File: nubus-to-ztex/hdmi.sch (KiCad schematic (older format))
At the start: 10 parts, among them J5 HDMI_A, U9 TPD12S016PWR

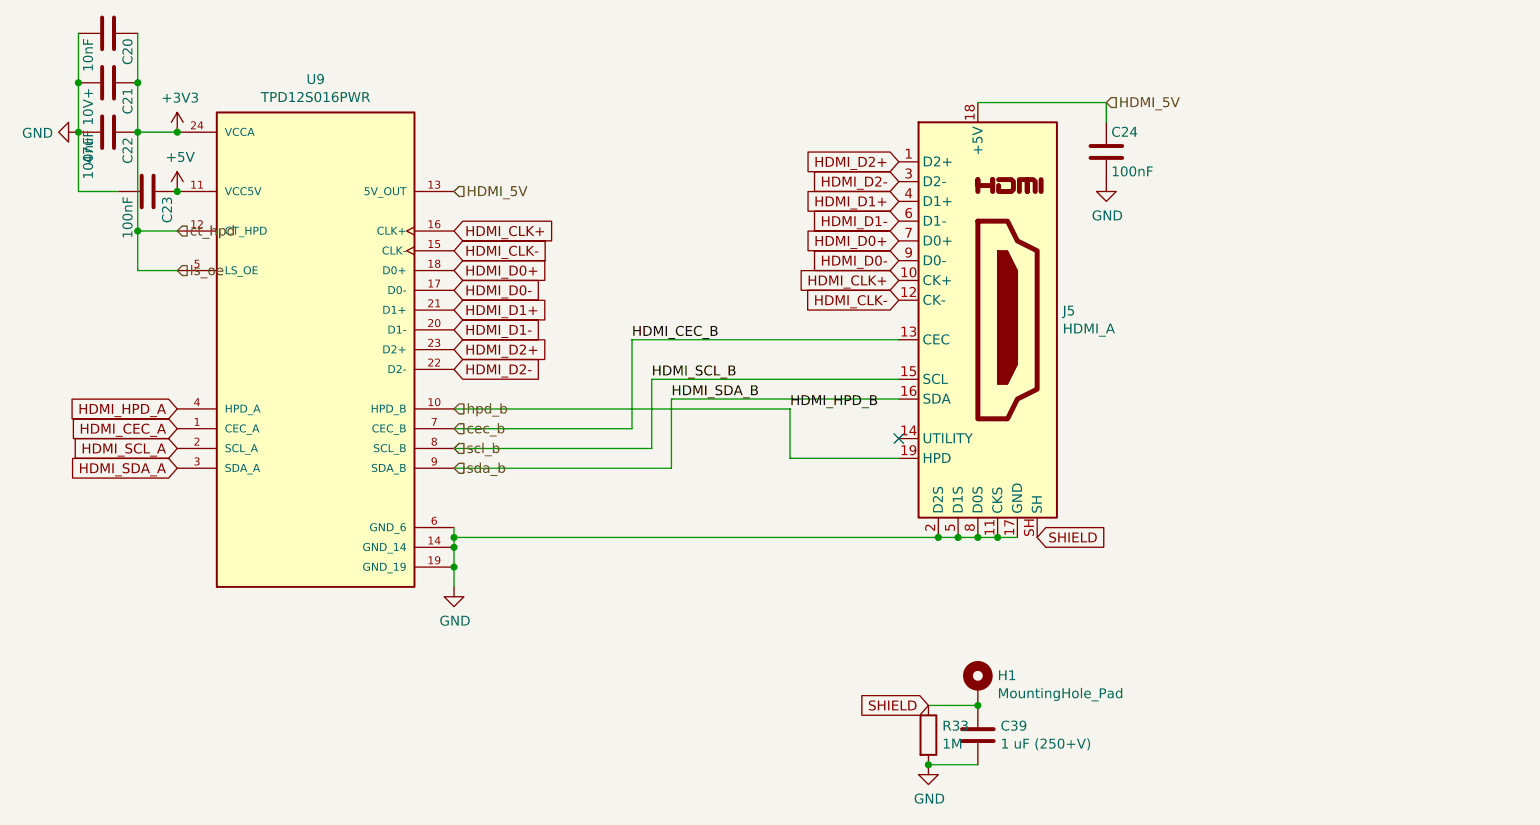
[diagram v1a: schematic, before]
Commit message: more update to V1.2 to try to limit cost
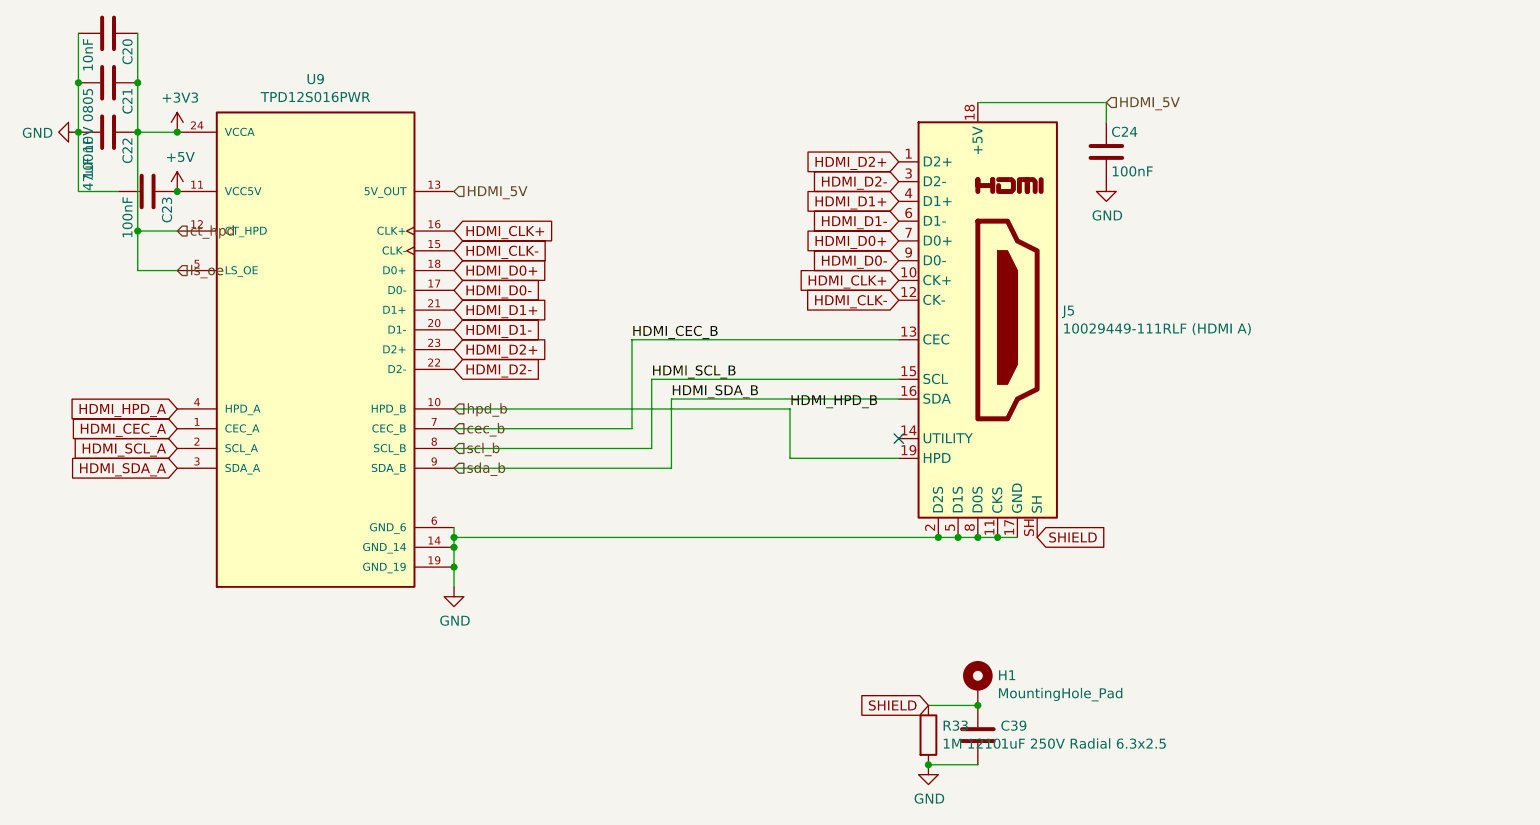
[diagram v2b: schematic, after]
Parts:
- C21: value 47uF 10V+ -> 47uF 10V 0805
- C39: value 1 uF (250+V) -> 1uF 250V Radial 6.3x2.5
- J5: value HDMI_A -> 10029449-111RLF (HDMI A)
- R33: value 1M -> 1M 1210
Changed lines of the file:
@@
 P 6650 2550
 F 0 "J5" H 7079 2596 50  0000 L CNN
-F 1 "HDMI_A" H 7079 2505 50  0000 L CNN
+F 1 "10029449-111RLF (HDMI A)" H 7079 2505 50  0000 L CNN
 F 2 "For_SeeedStudio:HDMI_A_Amphenol_10029449-111" H 6675 2550 50  0001 C CNN
 F 3 "https://en.wikipedia.org/wiki/HDMI" H 6675 2550 50  0001 C CNN
@@
 AR Path="/61B62C00/6148D34D" Ref="C21"  Part="1"
 F 0 "C21" H 2275 1450 50  0000 L CNN
-F 1 "47uF 10V+" H 2275 1250 50  0000 L CNN
+F 1 "47uF 10V 0805" H 2275 1250 50  0000 L CNN
 F 2 "Capacitor_SMD:C_0805_2012Metric" H 2288 1200 50  0001 C CNN
 F 3 "" H 2250 1350 50  0000 C CNN
@@
 AR Path="/61B62C00/63467FEB" Ref="C39"  Part="1"
 F 0 "C39" H 6765 4696 50  0000 L CNN
-F 1 "1 uF (250+V)" H 6765 4605 50  0000 L CNN
+F 1 "1uF 250V Radial 6.3x2.5" H 6765 4605 50  0000 L CNN
 F 2 "Capacitor_THT:CP_Radial_D6.3mm_P2.50mm" H 6688 4500 50  0001 C CNN
 F 3 "~" H 6650 4650 50  0001 C CNN
@@
 AR Path="/61B62C00/63467FF7" Ref="R33"  Part="1"
 F 0 "R33" H 6470 4696 50  0000 L CNN
-F 1 "1M" H 6470 4605 50  0000 L CNN
+F 1 "1M 1210" H 6470 4605 50  0000 L CNN
 F 2 "Resistor_SMD:R_1210_3225Metric" V 6330 4650 50  0001 C CNN
 F 3 "~" H 6400 4650 50  0001 C CNN

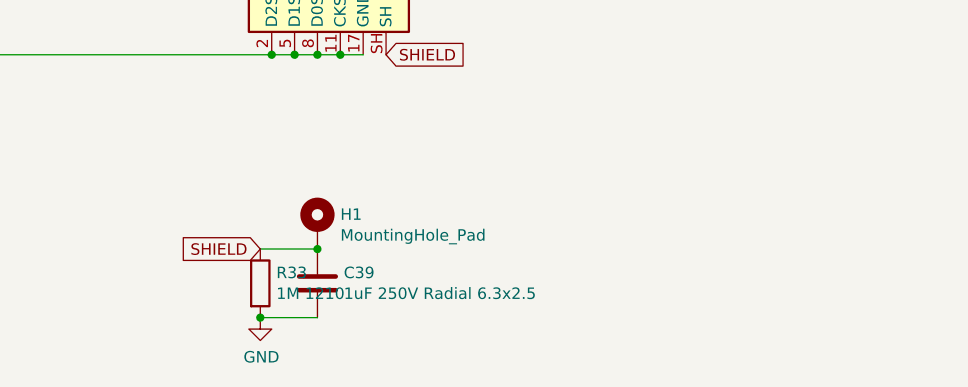
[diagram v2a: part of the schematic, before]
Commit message: more THT->SMT, lexx expensive parts/assembly (?)
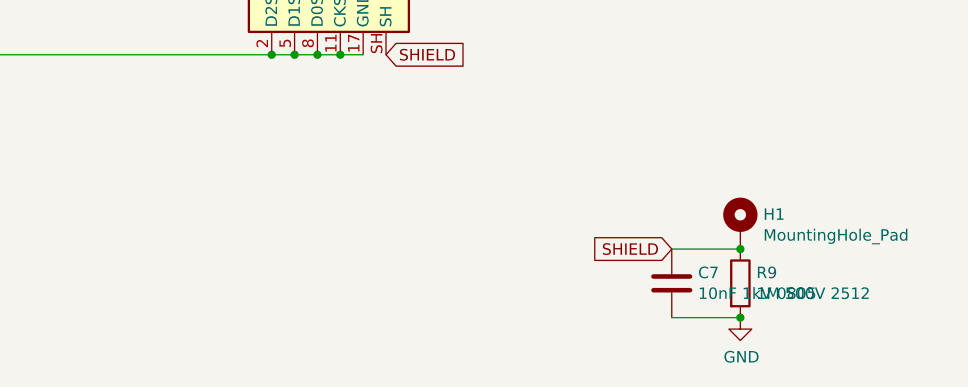
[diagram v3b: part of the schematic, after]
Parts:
- removed C39: 1uF 250V Radial 6.3x2.5, Capacitor_THT:CP_Radial_D6.3mm_P2.50mm, symbol Device:C
- removed R33: 1M 1210, Resistor_SMD:R_1210_3225Metric, symbol Device:R
- added C7: 10nF 1kV 0805, Capacitor_SMD:C_0805_2012Metric, symbol Device:C
- added R9: 1M 500V 2512, Resistor_SMD:R_2512_6332Metric, symbol Device:R
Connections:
- net GND: now also C7.2, R9.2
- net SHIELD: now also C7.1, R9.1
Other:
- moved on the sheet: H1
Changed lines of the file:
@@
 Text HLabel 4000 1900 2    50   Input ~ 0
 HDMI_5V
-Text GLabel 6400 4500 0    50   Input ~ 0
+Text GLabel 8200 4500 0    50   Input ~ 0
 SHIELD
 $Comp
+L Mechanical:MountingHole_Pad H?
+U 1 1 63467FFE
+P 8500 4400
+AR Path="/6193AB43/63467FFE" Ref="H?"  Part="1"
+AR Path="/61B62C00/63467FFE" Ref="H1"  Part="1"
+F 0 "H1" H 8600 4451 50  0000 L CNN
+F 1 "MountingHole_Pad" H 8600 4360 50  0000 L CNN
+F 2 "MountingHole:MountingHole_2.2mm_M2_Pad" H 8500 4400 50  0001 C CNN
+F 3 "~" H 8500 4400 50  0001 C CNN
+	1    8500 4400
+	1    0    0    -1
+$EndComp
+$Comp
 L power:GND #PWR?
-U 1 1 63467FDF
-P 6400 4800
-AR Path="/6193AB43/63467FDF" Ref="#PWR?"  Part="1"
-AR Path="/61B62C00/63467FDF" Ref="#PWR0132"  Part="1"
-F 0 "#PWR0132" H 6400 4550 50  0001 C CNN
-F 1 "GND" H 6405 4627 50  0000 C CNN
-F 2 "" H 6400 4800 50  0001 C CNN
-F 3 "" H 6400 4800 50  0001 C CNN
-	1    6400 4800
+U 1 1 641A2752
+P 8500 4800
+AR Path="/61B62C00/641A0A1A/641A2752" Ref="#PWR?"  Part="1"
+AR Path="/61B62C00/641A2752" Ref="#PWR0132"  Part="1"
+F 0 "#PWR0132" H 8500 4550 50  0001 C CNN
+F 1 "GND" H 8505 4627 50  0000 C CNN
+F 2 "" H 8500 4800 50  0001 C CNN
+F 3 "" H 8500 4800 50  0001 C CNN
+	1    8500 4800
+	1    0    0    -1
+$EndComp
+$Comp
+L Device:C C?
+U 1 1 641A275A
+P 8200 4650
+AR Path="/61B62C00/641A0A1A/641A275A" Ref="C?"  Part="1"
+AR Path="/61B62C00/641A275A" Ref="C7"  Part="1"
+F 0 "C7" H 8315 4696 50  0000 L CNN
+F 1 "10nF 1kV 0805" H 8315 4605 50  0000 L CNN
+F 2 "Capacitor_SMD:C_0805_2012Metric" H 8238 4500 50  0001 C CNN
+F 3 "~" H 8200 4650 50  0001 C CNN
+F 4 "C0805V103KCRACTU" H 8200 4650 50  0001 C CNN "MPN"
+F 5 "https://www.lcsc.com/product-detail/Multilayer-Ceramic-Capacitors-MLCC-SMD-SMT_KEMET-C0805V103KCRACTU_C2170011.html" H 8200 4650 50  0001 C CNN "URL"
+	1    8200 4650
 	1    0    0    -1
 $EndComp
 Wire Wire Line
-	6650 4800 6400 4800
-Wire Wire Line
-	6650 4500 6400 4500
+	8500 4800 8200 4800
 $Comp
-L Device:C C?
-U 1 1 63467FEB
-P 6650 4650
-AR Path="/6193AB43/63467FEB" Ref="C?"  Part="1"
-AR Path="/61B62C00/63467FEB" Ref="C39"  Part="1"
-F 0 "C39" H 6765 4696 50  0000 L CNN
-F 1 "1uF 250V Radial 6.3x2.5" H 6765 4605 50  0000 L CNN
-F 2 "Capacitor_THT:CP_Radial_D6.3mm_P2.50mm" H 6688 4500 50  0001 C CNN
-F 3 "~" H 6650 4650 50  0001 C CNN
-F 4 "860021373002" H 6650 4650 50  0001 C CNN "MPN-ALT"
-F 5 "https://www2.mouser.com/ProductDetail/Wurth-Elektronik/860021373002?qs=0KOYDY2FL28tNXbPyU6hsg%3D%3D" H 6650 4650 50  0001 C CNN "URL-ALT"
-F 6 "KM010M400E110A" H 6650 4650 50  0001 C CNN "MPN"
-F 7 "https://lcsc.com/product-detail/Aluminum-Electrolytic-Capacitors-Leaded_Capxon-International-Elec-KM010M400E110A_C59365.html" H 6650 4650 50  0001 C CNN "URL"
-	1    6650 4650
+L Device:R R?
+U 1 1 641A2763
+P 8500 4650
+AR Path="/61B62C00/641A0A1A/641A2763" Ref="R?"  Part="1"
+AR Path="/61B62C00/641A2763" Ref="R9"  Part="1"
+F 0 "R9" H 8570 4696 50  0000 L CNN
+F 1 "1M 500V 2512" H 8570 4605 50  0000 L CNN
+F 2 "Resistor_SMD:R_2512_6332Metric" V 8430 4650 50  0001 C CNN
+F 3 "~" H 8500 4650 50  0001 C CNN
+F 4 "AS25J1004ET" H 8500 4650 50  0001 C CNN "MPN"
+F 5 "https://www.lcsc.com/product-detail/Chip-Resistor-Surface-Mount_Ohmite-AS25J1004ET_C2546765.html" H 8500 4650 50  0001 C CNN "URL"
+	1    8500 4650
 	1    0    0    -1
 $EndComp
-Connection ~ 6400 4800
-$Comp
-L Device:R R?
-U 1 1 63467FF7
-P 6400 4650
-AR Path="/6193AB43/63467FF7" Ref="R?"  Part="1"
-AR Path="/61B62C00/63467FF7" Ref="R33"  Part="1"
-F 0 "R33" H 6470 4696 50  0000 L CNN
-F 1 "1M 1210" H 6470 4605 50  0000 L CNN
-F 2 "Resistor_SMD:R_1210_3225Metric" V 6330 4650 50  0001 C CNN
-F 3 "~" H 6400 4650 50  0001 C CNN
-F 4 "RC1210FR-071ML" H 6400 4650 50  0001 C CNN "MPN-ALT"
-F 5 "https://lcsc.com/product-detail/Chip-Resistor-Surface-Mount_YAGEO-RC1210FR-071ML_C470029.html" H 6400 4650 50  0001 C CNN "URL-ALT"
-F 6 "1210W2F1004T5E" H 6400 4650 50  0001 C CNN "MPN"
-F 7 "https://www.lcsc.com/product-detail/Chip-Resistor-Surface-Mount_UNI-ROYAL-Uniroyal-Elec-1210W2F1004T5E_C620664.html" H 6400 4650 50  0001 C CNN "URL"
-	1    6400 4650
-	1    0    0    -1
-$EndComp
-$Comp
-L Mechanical:MountingHole_Pad H?
-U 1 1 63467FFE
-P 6650 4400
-AR Path="/6193AB43/63467FFE" Ref="H?"  Part="1"
-AR Path="/61B62C00/63467FFE" Ref="H1"  Part="1"
-F 0 "H1" H 6750 4451 50  0000 L CNN
-F 1 "MountingHole_Pad" H 6750 4360 50  0000 L CNN
-F 2 "MountingHole:MountingHole_2.2mm_M2_Pad" H 6650 4400 50  0001 C CNN
-F 3 "~" H 6650 4400 50  0001 C CNN
-	1    6650 4400
-	1    0    0    -1
-$EndComp
-Connection ~ 6650 4500
+Connection ~ 8500 4800
+Wire Wire Line
+	8200 4500 8500 4500
+Connection ~ 8500 4500
 $EndSCHEMATC

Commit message: minor cleanups
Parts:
- C22, C23, C24: LCSC ? -> (none)
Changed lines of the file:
@@
 F 6 "603-CC603KRX7R8BB104" H 7300 1700 50  0001 C CNN "Mouser"
 F 7 "?" H 7300 1700 50  0001 C CNN "Digikey"
-F 8 "?" H 7300 1700 50  0001 C CNN "LCSC"
+F 8 "" H 7300 1700 50  0001 C CNN "LCSC"
 F 9 "?" H 7300 1700 50  0001 C CNN "Koncar"
 F 10 "TB" H 7300 1700 50  0001 C CNN "Side"
@@
 F 6 "603-CC603KRX7R8BB104" H 2250 1600 50  0001 C CNN "Mouser"
 F 7 "?" H 2250 1600 50  0001 C CNN "Digikey"
-F 8 "?" H 2250 1600 50  0001 C CNN "LCSC"
+F 8 "" H 2250 1600 50  0001 C CNN "LCSC"
 F 9 "?" H 2250 1600 50  0001 C CNN "Koncar"
 F 10 "TB" H 2250 1600 50  0001 C CNN "Side"
@@
 F 6 "603-CC603KRX7R8BB104" H 2450 1900 50  0001 C CNN "Mouser"
 F 7 "?" H 2450 1900 50  0001 C CNN "Digikey"
-F 8 "?" H 2450 1900 50  0001 C CNN "LCSC"
+F 8 "" H 2450 1900 50  0001 C CNN "LCSC"
 F 9 "?" H 2450 1900 50  0001 C CNN "Koncar"
 F 10 "TB" H 2450 1900 50  0001 C CNN "Side"

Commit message: BoM, power plane, serial back to THT, ...
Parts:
- C20, C22, C23, C24: URL https://lcsc.com/product-detail/Multilayer-Ceramic-Capacito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 -> https://www.lcsc.com/product-detail/Multilayer-Ceramic-Capa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
- C21: MPN GRM21BR61A476ME15K -> C2012X5R1A476MTJ00E; URL https://www.lcsc.com/product-detail/Multilayer-Ceramic-Capacitors-MLCC-SMD-SMT_Murata-Electronics-GRM21BR61A476ME15K_C2292827.html -> https://www.lcsc.com/product-detail/Multilayer-Ceramic-Capacitors-MLCC-SMD-SMT_TDK-C2012X5R1A476MTJ00E_C76636.html
- H1: DNP (none) -> DNP
- J5: URL https://lcsc.com/product-detail/D-Sub-DVI-HDMI-Connectors_A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 -> https://www.lcsc.com/product-detail/D-Sub-DVI-HDMI-Connecto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
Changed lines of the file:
@@
 F 9 "?" H 7300 1700 50  0001 C CNN "Koncar"
 F 10 "TB" H 7300 1700 50  0001 C CNN "Side"
-F 11 "https://lcsc.com/product-detail/Multilayer-Ceramic-Capacitors-MLCC-SMD-SMT_YAGEO-CC0603KRX7R8BB104_C92490.html" H 3000 6050 50  0001 C CNN "URL"
+F 11 "https://www.lcsc.com/product-detail/Multilayer-Ceramic-Capacitors-MLCC-SMD-SMT_YAGEO-CC0603KRX7R8BB104_C92490.html" H 3000 6050 50  0001 C CNN "URL"
 	1    7300 1700
 	1    0    0    -1
@@
 F 9 "?" H 2250 1600 50  0001 C CNN "Koncar"
 F 10 "TB" H 2250 1600 50  0001 C CNN "Side"
-F 11 "https://lcsc.com/product-detail/Multilayer-Ceramic-Capacitors-MLCC-SMD-SMT_YAGEO-CC0603KRX7R8BB104_C92490.html" H 2250 1600 50  0001 C CNN "URL"
+F 11 "https://www.lcsc.com/product-detail/Multilayer-Ceramic-Capacitors-MLCC-SMD-SMT_YAGEO-CC0603KRX7R8BB104_C92490.html" H 2250 1600 50  0001 C CNN "URL"
 	1    2250 1600
 	0    1    1    0
@@
 F 9 "?" H 2450 1900 50  0001 C CNN "Koncar"
 F 10 "TB" H 2450 1900 50  0001 C CNN "Side"
-F 11 "https://lcsc.com/product-detail/Multilayer-Ceramic-Capacitors-MLCC-SMD-SMT_YAGEO-CC0603KRX7R8BB104_C92490.html" H 3000 6050 50  0001 C CNN "URL"
+F 11 "https://www.lcsc.com/product-detail/Multilayer-Ceramic-Capacitors-MLCC-SMD-SMT_YAGEO-CC0603KRX7R8BB104_C92490.html" H 3000 6050 50  0001 C CNN "URL"
 	1    2450 1900
 	0    1    1    0
@@
 F 4 "10029449-111RLF" H 6650 2550 50  0001 C CNN "MPN"
 F 5 "https://www2.mouser.com/ProductDetail/Amphenol-FCI/10029449-111RLF?qs=fmpTyLOWOey0HPdD9%2F%2FaXA%3D%3D" H 6650 2550 50  0001 C CNN "URL-ALT"
-F 6 "https://lcsc.com/product-detail/D-Sub-DVI-HDMI-Connectors_Amphenol-ICC-10029449-111RLF_C427307.html" H 6650 2550 50  0001 C CNN "URL"
+F 6 "https://www.lcsc.com/product-detail/D-Sub-DVI-HDMI-Connectors_Amphenol-ICC-10029449-111RLF_C427307.html" H 6650 2550 50  0001 C CNN "URL"
 	1    6650 2550
 	1    0    0    -1
@@
 F 9 "https://www2.mouser.com/ProductDetail/?qs=u16ybLDytRYYQtTToF3RWA%3D%3D" H 2250 1350 50  0001 C CNN "URL-PREV"
 F 10 "https://lcsc.com/product-detail/Multilayer-Ceramic-Capacitors-MLCC-SMD-SMT_TDK-C2012X5R1A476MTJ00E_C76636.html" H 2250 1350 50  0001 C CNN "URL-ALT"
-F 11 "GRM21BR61A476ME15K" H 2250 1350 50  0001 C CNN "MPN"
-F 12 "https://www.lcsc.com/product-detail/Multilayer-Ceramic-Capacitors-MLCC-SMD-SMT_Murata-Electronics-GRM21BR61A476ME15K_C2292827.html" H 2250 1350 50  0001 C CNN "URL"
+F 11 "C2012X5R1A476MTJ00E" H 2250 1350 50  0001 C CNN "MPN"
+F 12 "https://www.lcsc.com/product-detail/Multilayer-Ceramic-Capacitors-MLCC-SMD-SMT_TDK-C2012X5R1A476MTJ00E_C76636.html" H 2250 1350 50  0001 C CNN "URL"
 	1    2250 1350
 	0    1    1    0
@@
 F 5 "CC0603KRX7R8BB103" H 2250 1100 50  0001 C CNN "MPN"
 F 6 "603-CC603KRX7R8BB103" H 2250 1100 50  0001 C CNN "Mouser"
-F 7 "https://lcsc.com/product-detail/Multilayer-Ceramic-Capacitors-MLCC-SMD-SMT_YAGEO-CC0603KRX7R8BB103_C327204.html" H 2250 1100 50  0001 C CNN "URL"
+F 7 "https://www.lcsc.com/product-detail/Multilayer-Ceramic-Capacitors-MLCC-SMD-SMT_YAGEO-CC0603KRX7R8BB103_C327204.html" H 2250 1100 50  0001 C CNN "URL"
 	1    2250 1100
 	0    1    1    0
@@
 F 2 "MountingHole:MountingHole_2.2mm_M2_Pad" H 8500 4400 50  0001 C CNN
 F 3 "~" H 8500 4400 50  0001 C CNN
+F 4 "DNP" H 8500 4400 50  0001 C CNN "DNP"
 	1    8500 4400
 	1    0    0    -1
